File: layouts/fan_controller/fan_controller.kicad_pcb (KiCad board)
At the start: 2 copper layers, 6 parts

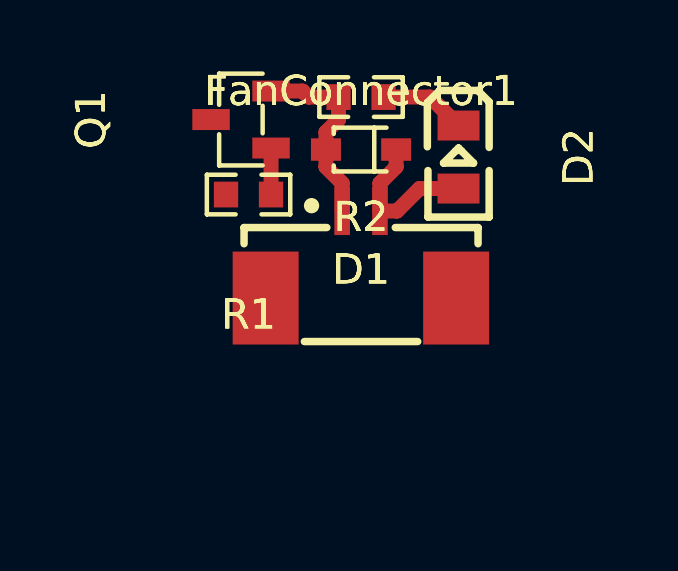
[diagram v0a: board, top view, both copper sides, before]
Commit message: Make it build with ato 0.8.x
- refactor modules
- clean up modules and structure
- convert some from fabll to ato
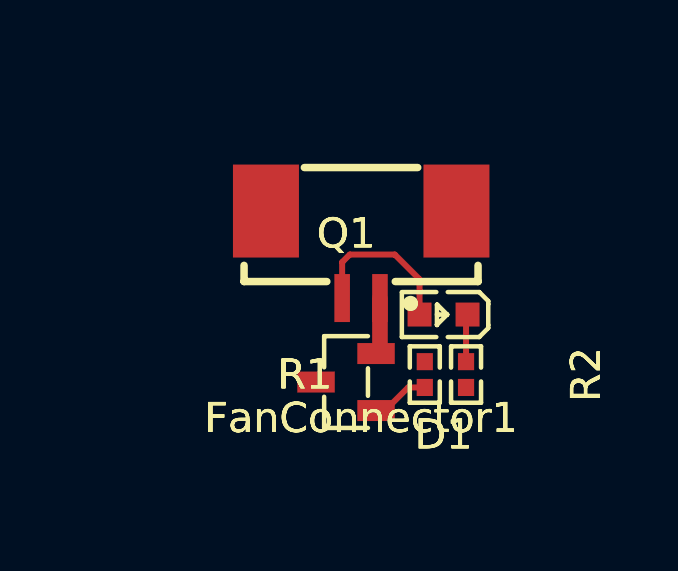
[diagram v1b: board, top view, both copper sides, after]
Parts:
- removed D2: , atopile:LED0805-R-RD-d1137b
- D1: value 450mV -> 2V; footprint atopile:SOD-323_L1.8-W1.3-LS2.5-RD-b55baa -> lib:LED0603-RD
- Q1: footprint atopile:SOT-23-3_L2.9-W1.3-P1.90-LS2.4-BL-1-fcaf94 -> atopile:SOT-23-3_L2.9-W1.3-P1.90-LS2.4-BR-688f29
- R1: value 10kΩ ±1% 100mW -> 10kΩ ±1% 62.5mW; footprint atopile:R0603-ebcab9 -> atopile:R0402-56259e
- R2: value 10kΩ ±1% 100mW -> 1kΩ ±1% 62.5mW; footprint atopile:R0603-ebcab9 -> atopile:R0402-56259e
- moved R2 9.89 mm to (3.50, 4.00), turned to -90 degrees
- moved Q1 9.42 mm to (-0.50, 4.25), turned to 0 degrees
- moved R1 8.40 mm to (2.12, 4.00), turned to 90 degrees
- moved D1 6.15 mm to (2.75, 2.00)
- turned FanConnector1 to 180 degrees
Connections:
- net line renamed gate
- D1 pad 1: hv -> cathode
- D1 pad 2: gnd -> anode
- FanConnector1 pad 2: hv -> anode
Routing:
- net anode: track 0.00 -> 5.40 mm
- net hv: track 5.20 -> 0.00 mm
- net gnd: track 6.53 -> 1.90 mm
- net cathode: track 2.89 -> 1.59 mm

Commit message: Finish layout, swap to ufl version of esp32c3
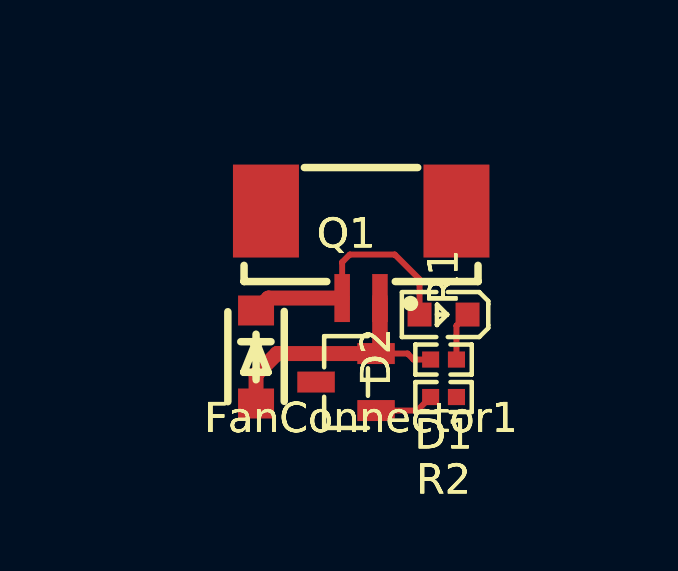
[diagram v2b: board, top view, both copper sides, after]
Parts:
- added D2: , atopile:SOD-123F_L2.8-W1.8-LS3.7-RD-7788aa, F.Cu at (-3.50, 3.42)
- moved R1 0.98 mm to (2.75, 4.75), turned to 0 degrees
- moved R2 0.90 mm to (2.75, 3.50), turned to 180 degrees
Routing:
- net gnd: track 1.90 -> 9.06 mm
- net anode: track 5.40 -> 8.44 mm
